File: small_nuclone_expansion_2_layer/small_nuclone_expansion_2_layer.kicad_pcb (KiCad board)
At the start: 2 copper layers, 48.3 x 48.3 mm, 11 parts, among them J1 nuclone_small_left, J2 nuclone_small_right, J3 PINS_1X18, J4 PINS_1X17

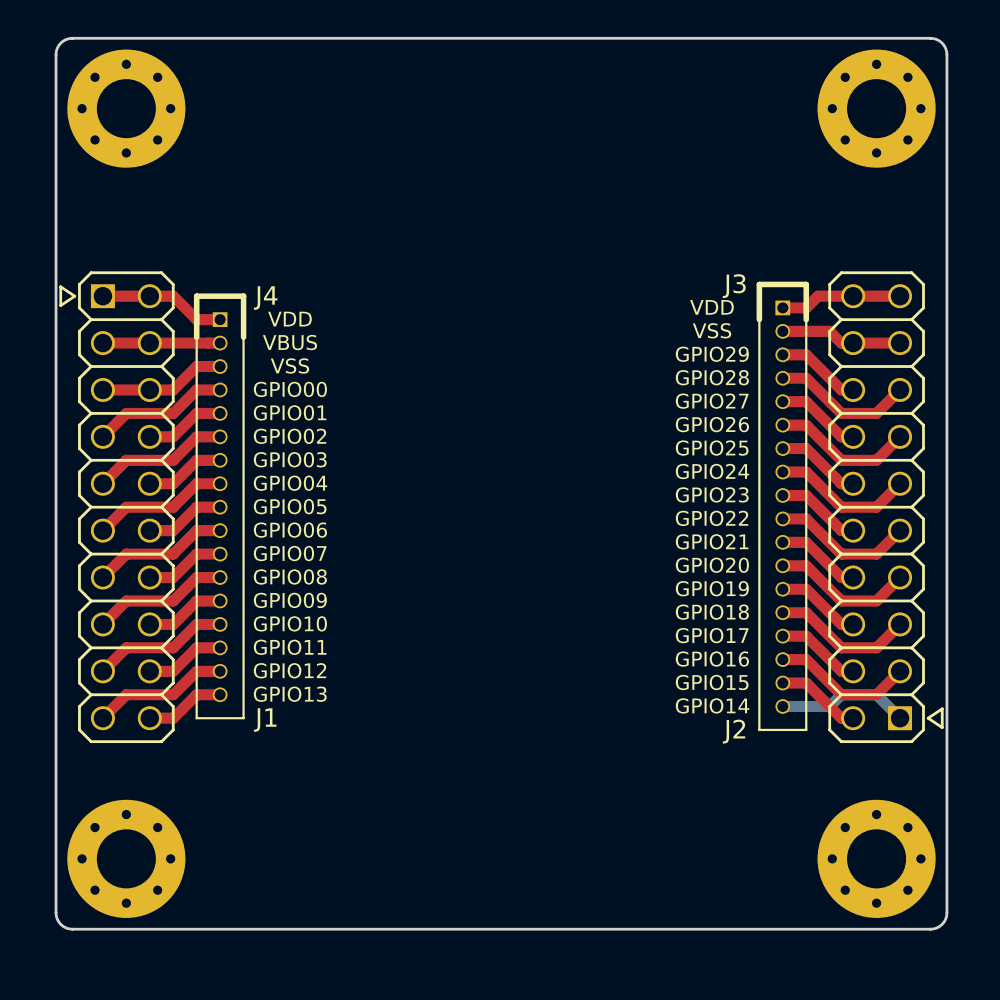
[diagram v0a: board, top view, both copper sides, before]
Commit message: updated small nuclone expansion board template with new mechanical outline
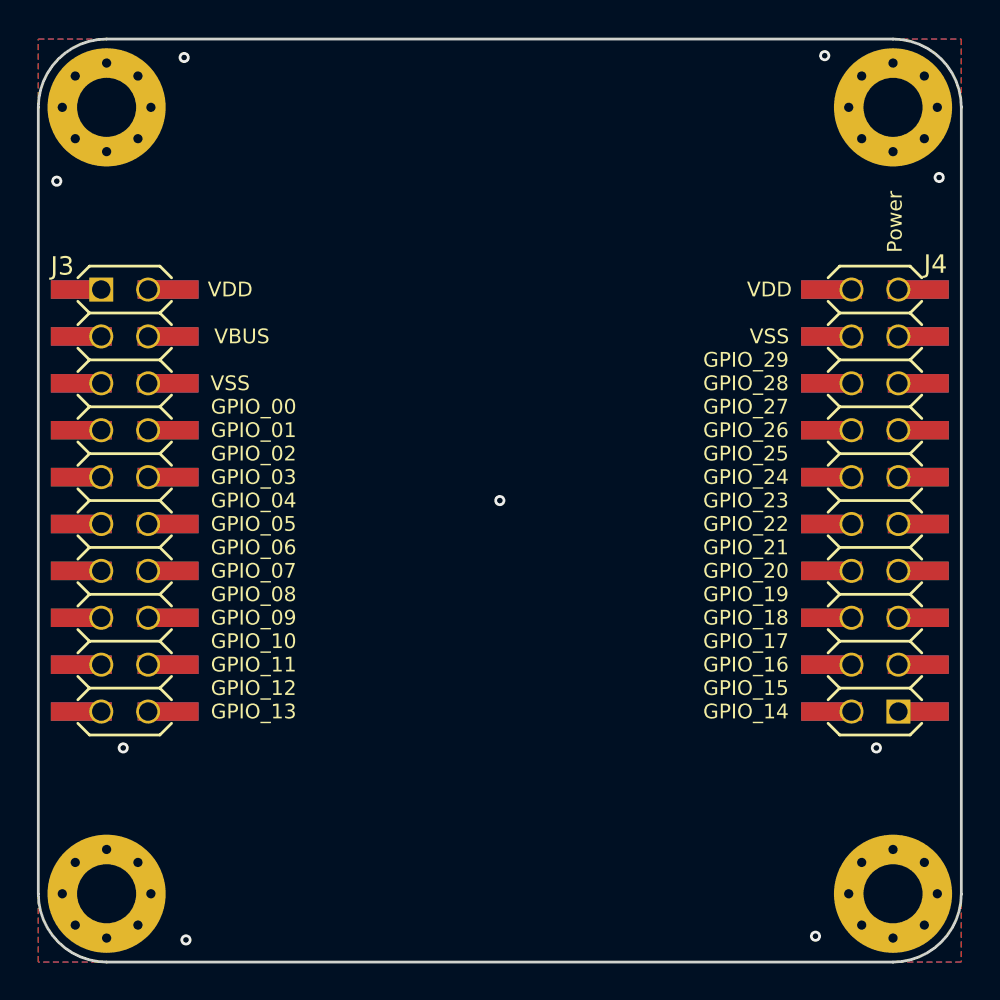
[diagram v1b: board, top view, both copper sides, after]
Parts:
- removed J1: nuclone_small_left, SquantorConnectors:Header-0254-2X10-H010
- removed J2: nuclone_small_right, SquantorConnectors:Header-0254-2X10-H010
- J3: value PINS_1X18 -> nuclone_small_left; footprint SquantorConnectors:Header-0127-1X18-H006 -> SquantorConnectorsNamed:nuclone_small_left_stacked
- J4: value PINS_1X17 -> nuclone_small_right; footprint SquantorConnectors:Header-0127-1X17-H006 -> SquantorConnectorsNamed:nuclone_small_right_stacked
- N1: footprint Symbol:OSHW-Symbol_6.7x6mm_SilkScreen -> Symbols:OSHW-Symbol_6.7x6mm_SilkScreen
- N2: value 20200808 -> V20220215
- moved J3 35.7 mm to (64.7, 86.0)
- moved J4 35.5 mm to (105.3, 86.0), turned to 90 degrees
- moved H4 2.17 mm to (63.7, 107.3)
- moved H3 2.09 mm to (106.3, 107.3)
- moved N2 1.98 mm to (85.0, 107.4), turned to 180 degrees
- moved N1 1.78 mm to (84.8, 103.7)
- moved N3 1.49 mm to (84.9, 108.9)
- moved H1 1.07 mm to (63.7, 64.7)
- moved H2 0.89 mm to (106.3, 64.7)
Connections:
- J3 pad 1: /VDD2 -> /VDD
- J3 pad 10: /GPIO_22 -> /GPIO_03
- J3 pad 11: /GPIO_21 -> /GPIO_04
- J3 pad 12: /GPIO_20 -> /GPIO_05
- J3 pad 13: /GPIO_19 -> /GPIO_06
- J3 pad 14: /GPIO_18 -> /GPIO_07
- J3 pad 15: /GPIO_17 -> /GPIO_08
- J3 pad 16: /GPIO_16 -> /GPIO_09
- J3 pad 17: /GPIO_15 -> /GPIO_10
- J3 pad 18: /GPIO_14 -> /GPIO_11
- J3 pad 2: /VSS2 -> /VDD
- J3 pad 3: /GPIO_29 -> /VBUS
- J3 pad 4: /GPIO_28 -> /VBUS
- J3 pad 5: /GPIO_27 -> /VSS
- J3 pad 6: /GPIO_26 -> /VSS
- J3 pad 7: /GPIO_25 -> /GPIO_00
- J3 pad 8: /GPIO_24 -> /GPIO_01
- J3 pad 9: /GPIO_23 -> /GPIO_02
- J4 pad 1: /VDD1 -> /GPIO_15
- J4 pad 10: /GPIO_06 -> /GPIO_22
- J4 pad 11: /GPIO_07 -> /GPIO_25
- J4 pad 12: /GPIO_08 -> /GPIO_24
- J4 pad 13: /GPIO_09 -> /GPIO_27
- J4 pad 14: /GPIO_10 -> /GPIO_26
- J4 pad 15: /GPIO_11 -> /GPIO_29
- J4 pad 16: /GPIO_12 -> /GPIO_28
- J4 pad 17: /GPIO_13 -> /VSS
- J4 pad 2: /VBUS -> /GPIO_14
- J4 pad 3: /VSS1 -> /GPIO_17
- J4 pad 4: /GPIO_00 -> /GPIO_16
- J4 pad 5: /GPIO_01 -> /GPIO_19
- J4 pad 6: /GPIO_02 -> /GPIO_18
- J4 pad 7: /GPIO_03 -> /GPIO_21
- J4 pad 8: /GPIO_04 -> /GPIO_20
- J4 pad 9: /GPIO_05 -> /GPIO_23
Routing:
- net /GPIO_22: track 7.67 -> 0.00 mm
- net /GPIO_18: track 7.67 -> 0.00 mm
- net /GPIO_28: track 7.67 -> 0.00 mm
- net /GPIO_24: track 7.67 -> 0.00 mm
- net /GPIO_20: track 7.67 -> 0.00 mm
- net /GPIO_16: track 7.67 -> 0.00 mm
- net /GPIO_26: track 7.67 -> 0.00 mm
- net /VDD1: track 7.51 -> 0.00 mm
- net /GPIO_12: track 7.40 -> 0.00 mm
- net /GPIO_10: track 7.40 -> 0.00 mm
- net /GPIO_06: track 7.40 -> 0.00 mm
- net /GPIO_02: track 7.40 -> 0.00 mm
- net /GPIO_08: track 7.40 -> 0.00 mm
- net /GPIO_04: track 7.40 -> 0.00 mm
- net /GPIO_00: track 7.40 -> 0.00 mm
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- added copper zone on B.Cu, net /VSS
- added copper zone on F.Cu, net /VSS
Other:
- board size 48.3 x 48.3 mm -> 50 x 50 mm
- net class Default: clearance 0.127 -> 0.1; trace_width 0.127 -> 0.2
- net class Power added: clearance 0.1, trace_width 0.6, via_dia 1.1, via_drill 0.8
- net class Signal added: clearance 0.1, trace_width 0.3, via_dia 0.6, via_drill 0.3
- rule pad_to_mask_clearance: 0.1 -> 0
- rule trace_clearance: 0.127 -> 0.1
- board text added: "Power"
- board text removed: "GPIO00"
- board text removed: "GPIO01"
- board text removed: "GPIO02"
- board text removed: "GPIO03"
- board text removed: "GPIO04"
- board text removed: "GPIO05"
- board text removed: "GPIO06"
- board text removed: "GPIO07"
- board text removed: "GPIO08"
- board text removed: "GPIO09"
- board text removed: "GPIO10"
- board text removed: "GPIO11"
- board text removed: "GPIO12"
- board text removed: "GPIO13"
- board text removed: "GPIO14"
- board text removed: "GPIO15"
- board text removed: "GPIO16"
- board text removed: "GPIO17"
- board text removed: "GPIO18"
- board text removed: "GPIO19"
- board text removed: "GPIO20"
- board text removed: "GPIO21"
- board text removed: "GPIO22"
- board text removed: "GPIO23"
- board text removed: "GPIO24"
- board text removed: "GPIO25"
- board text removed: "GPIO26"
- board text removed: "GPIO27"
- board text removed: "GPIO28"
- board text removed: "GPIO29"
- board text removed: "VBUS"
- board text removed: "VDD"
- board text removed: "VSS"

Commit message: started with first breakout testpoints
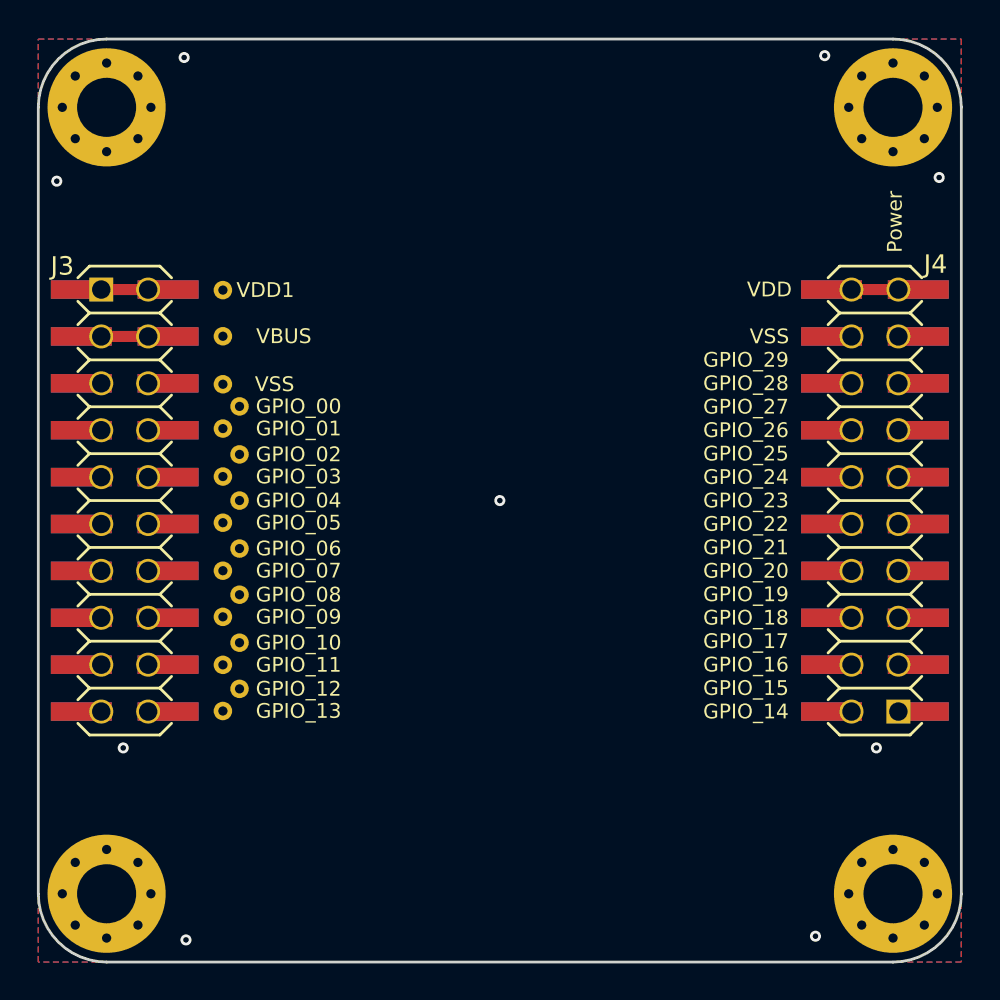
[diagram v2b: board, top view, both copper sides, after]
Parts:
- added TP1: VDD1, SquantorTestPoints:TestPoint_hole_H05R10_small_text, F.Cu at (70.0, 74.6)
- added TP10: GPIO_06, SquantorTestPoints:TestPoint_hole_H05R10_small_text, F.Cu at (70.9, 88.6)
- added TP11: GPIO_07, SquantorTestPoints:TestPoint_hole_H05R10_small_text, F.Cu at (70.0, 89.8)
- added TP12: GPIO_08, SquantorTestPoints:TestPoint_hole_H05R10_small_text, F.Cu at (70.9, 91.1)
- added TP13: GPIO_09, SquantorTestPoints:TestPoint_hole_H05R10_small_text, F.Cu at (70.0, 92.3)
- added TP14: GPIO_10, SquantorTestPoints:TestPoint_hole_H05R10_small_text, F.Cu at (70.9, 93.7)
- added TP15: GPIO_11, SquantorTestPoints:TestPoint_hole_H05R10_small_text, F.Cu at (70.0, 94.9)
- added TP16: GPIO_12, SquantorTestPoints:TestPoint_hole_H05R10_small_text, F.Cu at (70.9, 96.2)
- added TP17: GPIO_13, SquantorTestPoints:TestPoint_hole_H05R10_small_text, F.Cu at (70.0, 97.4)
- added TP2: VBUS, SquantorTestPoints:TestPoint_hole_H05R10_small_text, F.Cu at (70.0, 77.1)
- added TP3: VSS, SquantorTestPoints:TestPoint_hole_H05R10_small_text, F.Cu at (70.0, 79.7)
- added TP4: GPIO_00, SquantorTestPoints:TestPoint_hole_H05R10_small_text, F.Cu at (70.9, 80.9)
- added TP5: GPIO_01, SquantorTestPoints:TestPoint_hole_H05R10_small_text, F.Cu at (70.0, 82.1)
- added TP6: GPIO_02, SquantorTestPoints:TestPoint_hole_H05R10_small_text, F.Cu at (70.9, 83.5)
- added TP7: GPIO_03, SquantorTestPoints:TestPoint_hole_H05R10_small_text, F.Cu at (70.0, 84.7)
- added TP8: GPIO_04, SquantorTestPoints:TestPoint_hole_H05R10_small_text, F.Cu at (70.9, 86.0)
- added TP9: GPIO_05, SquantorTestPoints:TestPoint_hole_H05R10_small_text, F.Cu at (70.0, 87.2)
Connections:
- J3 pad 1: /VDD -> /VDD1
- J3 pad 2: /VDD -> /VDD1
- J4 pad 19: /VDD -> /VDD2
- J4 pad 20: /VDD -> /VDD2
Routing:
- net /VDD2: track 0.00 -> 4.70 mm
- net /VDD1: track 0.00 -> 4.70 mm
- net /VBUS: track 0.00 -> 4.70 mm

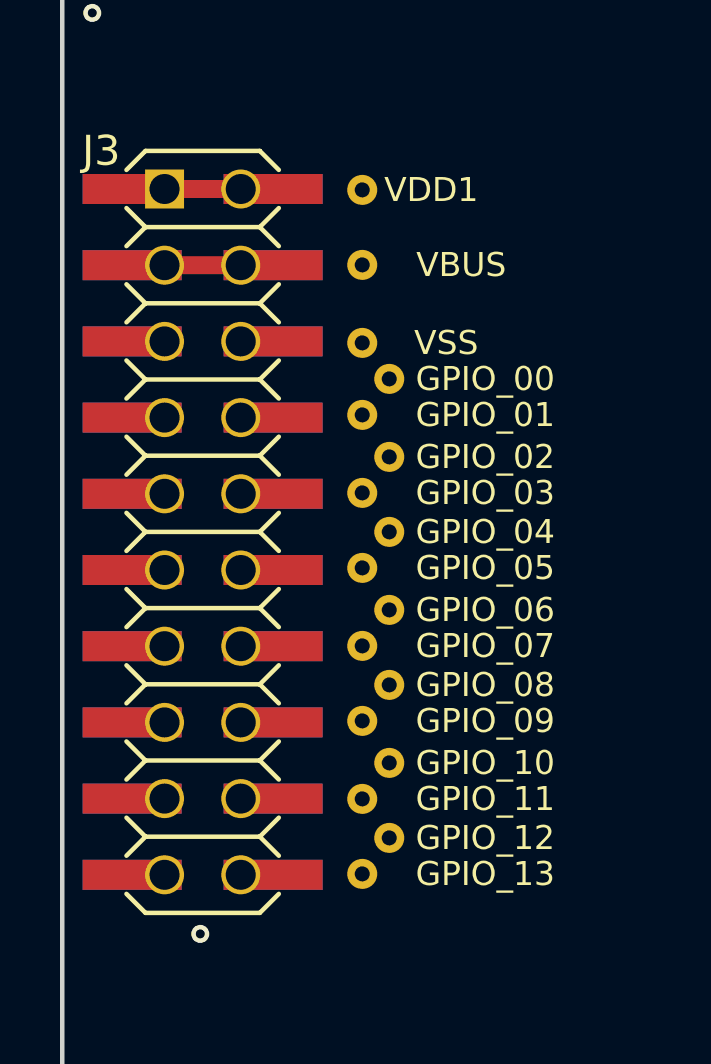
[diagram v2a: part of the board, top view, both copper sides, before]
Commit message: routed left testpoints
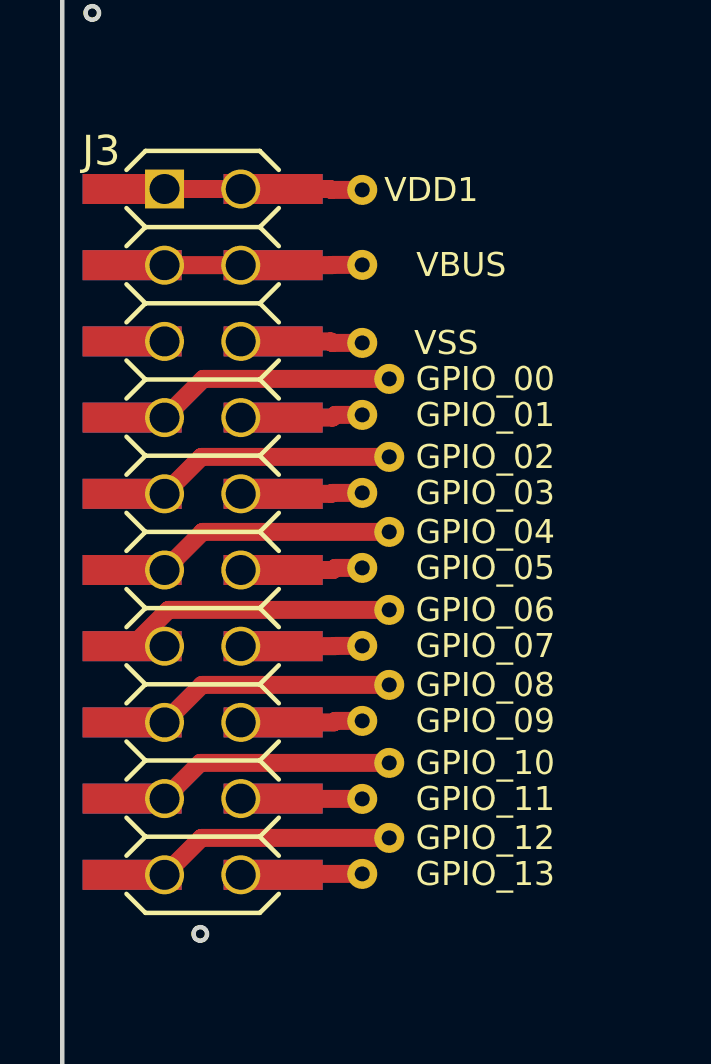
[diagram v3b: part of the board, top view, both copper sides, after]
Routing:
- net /GPIO_06: track 0.00 -> 9.07 mm
- net /GPIO_00: track 0.00 -> 8.02 mm
- net /GPIO_04: track 0.00 -> 8.02 mm
- net /GPIO_08: track 0.00 -> 8.01 mm
- net /GPIO_12: track 0.00 -> 8.00 mm
- net /GPIO_02: track 0.00 -> 8.00 mm
- net /GPIO_10: track 0.00 -> 7.98 mm
- net /GPIO_01: track 0.00 -> 3.01 mm
- net /GPIO_05: track 0.00 -> 3.00 mm
- net /VSS: track 0.00 -> 2.99 mm
- net /GPIO_09: track 0.00 -> 2.99 mm
- net /VDD1: track 4.70 -> 7.68 mm
- net /GPIO_13: track 0.00 -> 2.98 mm
- net /GPIO_03: track 0.00 -> 2.98 mm
- net /GPIO_07: track 0.00 -> 2.97 mm
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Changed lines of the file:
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@@
     (thickness 1.6)
     (drawings 19)
-    (tracks 12)
+    (tracks 54)
     (zones 0)
     (modules 26)
@@
   (gr_line (start 60 64.7) (end 60 107.3) (layer Edge.Cuts) (width 0.15))
   (segment (start 62.33 77.11) (end 67.03 77.11) (width 0.6) (layer F.Cu) (net 1))
+  (segment (start 68.99 77.11) (end 67.03 77.11) (width 0.6) (layer F.Cu) (net 1))
+  (segment (start 69 77.1) (end 68.99 77.11) (width 0.6) (layer F.Cu) (net 1))
+  (segment (start 70 77.1) (end 69 77.1) (width 0.6) (layer F.Cu) (net 1))
   (via (at 64.6 99.4) (size 0.6) (drill 0.3) (layers F.Cu B.Cu) (net 2))
   (via (at 105.4 99.4) (size 0.6) (drill 0.3) (layers F.Cu B.Cu) (net 2))
@@
   (via (at 102.6 61.9) (size 0.6) (drill 0.3) (layers F.Cu B.Cu) (net 2))
   (via (at 108.8 68.5) (size 0.6) (drill 0.3) (layers F.Cu B.Cu) (net 2))
+  (segment (start 70 79.7) (end 69 79.7) (width 0.6) (layer F.Cu) (net 2))
+  (segment (start 68.95 79.65) (end 67.03 79.65) (width 0.6) (layer F.Cu) (net 2))
+  (segment (start 69 79.7) (end 68.95 79.65) (width 0.6) (layer F.Cu) (net 2))
+  (segment (start 67.06 97.4) (end 67.03 97.43) (width 0.6) (layer F.Cu) (net 19))
+  (segment (start 70 97.4) (end 67.06 97.4) (width 0.6) (layer F.Cu) (net 19))
+  (segment (start 64.64 96.2) (end 63.41 97.43) (width 0.6) (layer F.Cu) (net 20))
+  (segment (start 70.9 96.2) (end 64.64 96.2) (width 0.6) (layer F.Cu) (net 20))
+  (segment (start 67.04 94.9) (end 67.03 94.89) (width 0.6) (layer F.Cu) (net 21))
+  (segment (start 70 94.9) (end 67.04 94.9) (width 0.6) (layer F.Cu) (net 21))
+  (segment (start 64.6 93.7) (end 63.41 94.89) (width 0.6) (layer F.Cu) (net 22))
+  (segment (start 70.9 93.7) (end 64.6 93.7) (width 0.6) (layer F.Cu) (net 22))
+  (segment (start 70 92.3) (end 69.1 92.3) (width 0.6) (layer F.Cu) (net 23))
+  (segment (start 69.05 92.35) (end 67.03 92.35) (width 0.6) (layer F.Cu) (net 23))
+  (segment (start 69.1 92.3) (end 69.05 92.35) (width 0.6) (layer F.Cu) (net 23))
+  (segment (start 64.66 91.1) (end 63.41 92.35) (width 0.6) (layer F.Cu) (net 24))
+  (segment (start 70.9 91.1) (end 64.66 91.1) (width 0.6) (layer F.Cu) (net 24))
+  (segment (start 70 89.8) (end 69.1 89.8) (width 0.6) (layer F.Cu) (net 25))
+  (segment (start 69.09 89.81) (end 67.03 89.81) (width 0.6) (layer F.Cu) (net 25))
+  (segment (start 69.1 89.8) (end 69.09 89.81) (width 0.6) (layer F.Cu) (net 25))
+  (segment (start 63.54 88.6) (end 62.33 89.81) (width 0.6) (layer F.Cu) (net 26))
+  (segment (start 70.9 88.6) (end 63.54 88.6) (width 0.6) (layer F.Cu) (net 26))
+  (segment (start 70 87.2) (end 69.1 87.2) (width 0.6) (layer F.Cu) (net 27))
+  (segment (start 69.03 87.27) (end 67.03 87.27) (width 0.6) (layer F.Cu) (net 27))
+  (segment (start 69.1 87.2) (end 69.03 87.27) (width 0.6) (layer F.Cu) (net 27))
+  (segment (start 64.68 86) (end 63.41 87.27) (width 0.6) (layer F.Cu) (net 28))
+  (segment (start 70.9 86) (end 64.68 86) (width 0.6) (layer F.Cu) (net 28))
+  (segment (start 70 84.7) (end 69 84.7) (width 0.6) (layer F.Cu) (net 29))
+  (segment (start 68.97 84.73) (end 67.03 84.73) (width 0.6) (layer F.Cu) (net 29))
+  (segment (start 69 84.7) (end 68.97 84.73) (width 0.6) (layer F.Cu) (net 29))
+  (segment (start 64.64 83.5) (end 63.41 84.73) (width 0.6) (layer F.Cu) (net 30))
+  (segment (start 70.9 83.5) (end 64.64 83.5) (width 0.6) (layer F.Cu) (net 30))
+  (segment (start 70 82.1) (end 69.1 82.1) (width 0.6) (layer F.Cu) (net 31))
+  (segment (start 69.01 82.19) (end 67.03 82.19) (width 0.6) (layer F.Cu) (net 31))
+  (segment (start 69.1 82.1) (end 69.01 82.19) (width 0.6) (layer F.Cu) (net 31))
+  (segment (start 64.7 80.9) (end 63.41 82.19) (width 0.6) (layer F.Cu) (net 32))
+  (segment (start 70.9 80.9) (end 64.7 80.9) (width 0.6) (layer F.Cu) (net 32))
   (segment (start 62.33 74.57) (end 67.03 74.57) (width 0.6) (layer F.Cu) (net 33))
+  (segment (start 68.93 74.57) (end 67.03 74.57) (width 0.6) (layer F.Cu) (net 33))
+  (segment (start 68.96 74.6) (end 68.93 74.57) (width 0.6) (layer F.Cu) (net 33))
+  (segment (start 70 74.6) (end 68.96 74.6) (width 0.6) (layer F.Cu) (net 33))
   (segment (start 107.67 74.57) (end 102.97 74.57) (width 0.6) (layer F.Cu) (net 34))
   (zone (net 2) (net_name /VSS) (layer B.Cu) (hatch edge 0.508)
